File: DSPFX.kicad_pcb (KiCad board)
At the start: 2 copper layers, 182.8 x 128.5 mm, 151 parts, among them J10 Conn_02x05_Odd_Even, J101 AudioJack2, J102 AudioJack2, J103 AudioJack2, J104 AudioJack2, J105 Conn_02x04_Odd_Even, J106 AudioJack2, J107 AudioJack2, J108 AudioJack2, J109 AudioJack2, J110 AudioJack2, J111 AudioJack2, J112 AudioJack2, J113 AudioJack2_SwitchT, J114 Conn_02x04_Odd_Even, J115 Conn_01x04_Pin, J116 Conn_01x04_Pin, J117 Conn_01x04_Pin, J118 Conn_01x04_Pin, J119 Conn_01x04_Pin, J120 Conn_01x04_Pin, J121 Conn_01x03_Pin, J122 Conn_01x04_Pin, J123 Conn_01x02_Pin, J124 Conn_01x02_Pin, J125 Conn_01x03_Pin, J126 Conn_01x04_Pin, J127 Conn_01x04_Pin, J128 Conn_01x04_Pin, Q101 BC847, Q102 BC847, Q103 BC847, Q104 BC847, SW101 SW_Push, SW102 SW_Push, U101 TL074, U102 MCP6004, U104 TL072, U105 7Segment, U106 LM337_SOT223, U107 DSP32-CORE

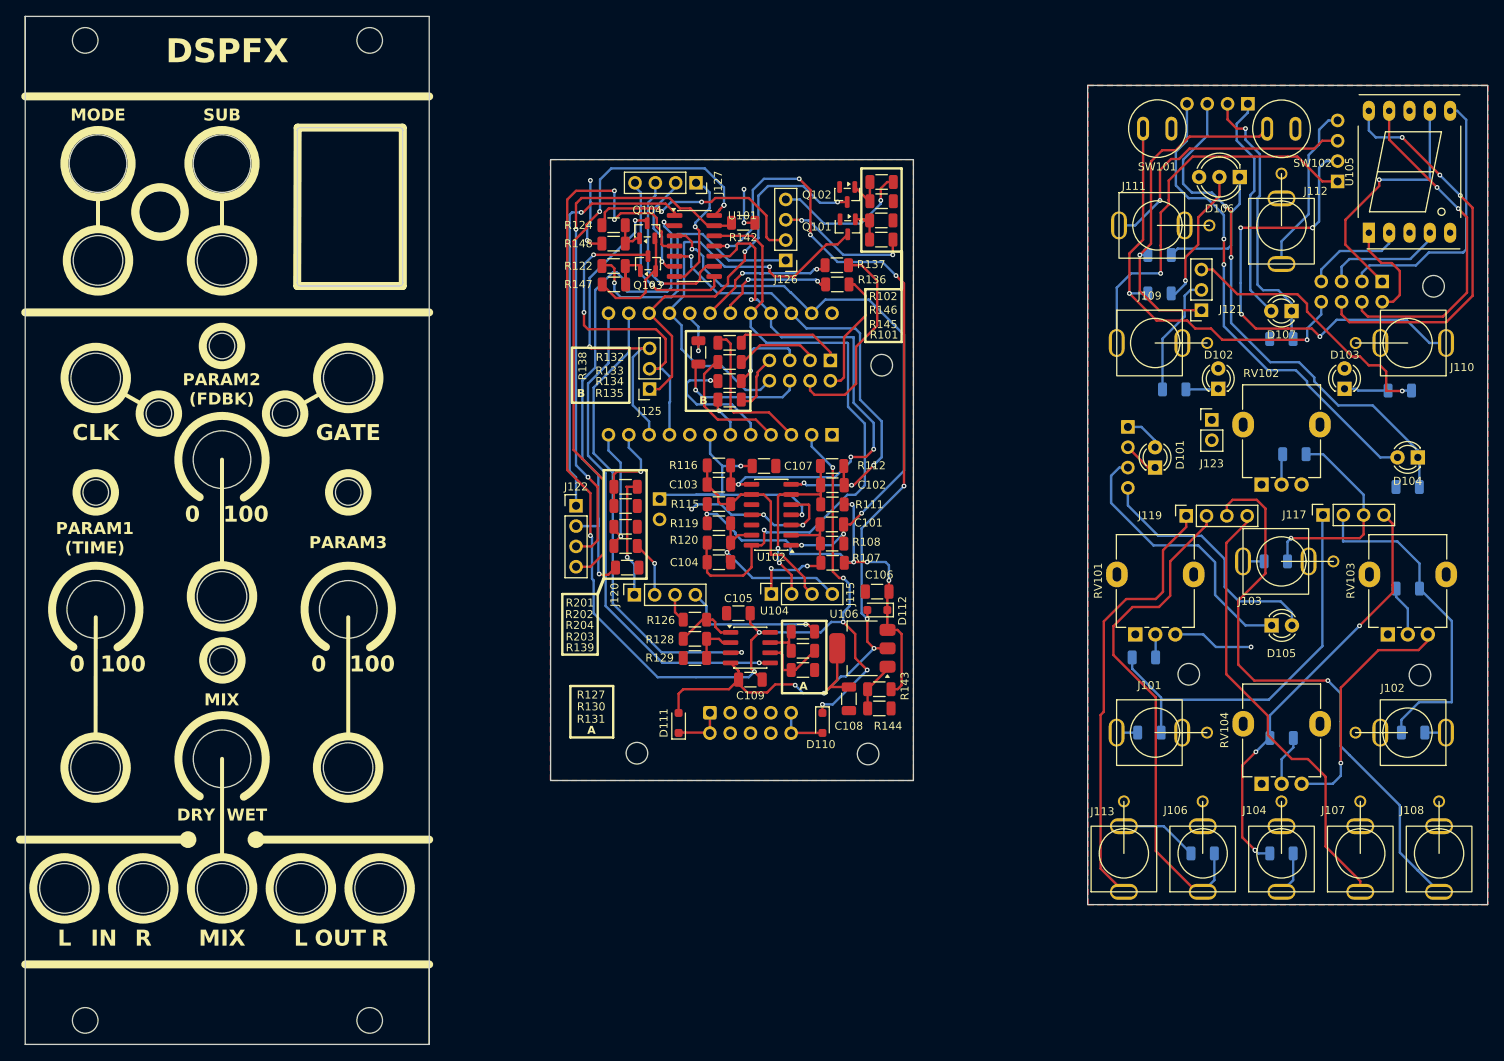
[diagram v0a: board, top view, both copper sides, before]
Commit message: Swapped LEDs and Potentiometer parity issue
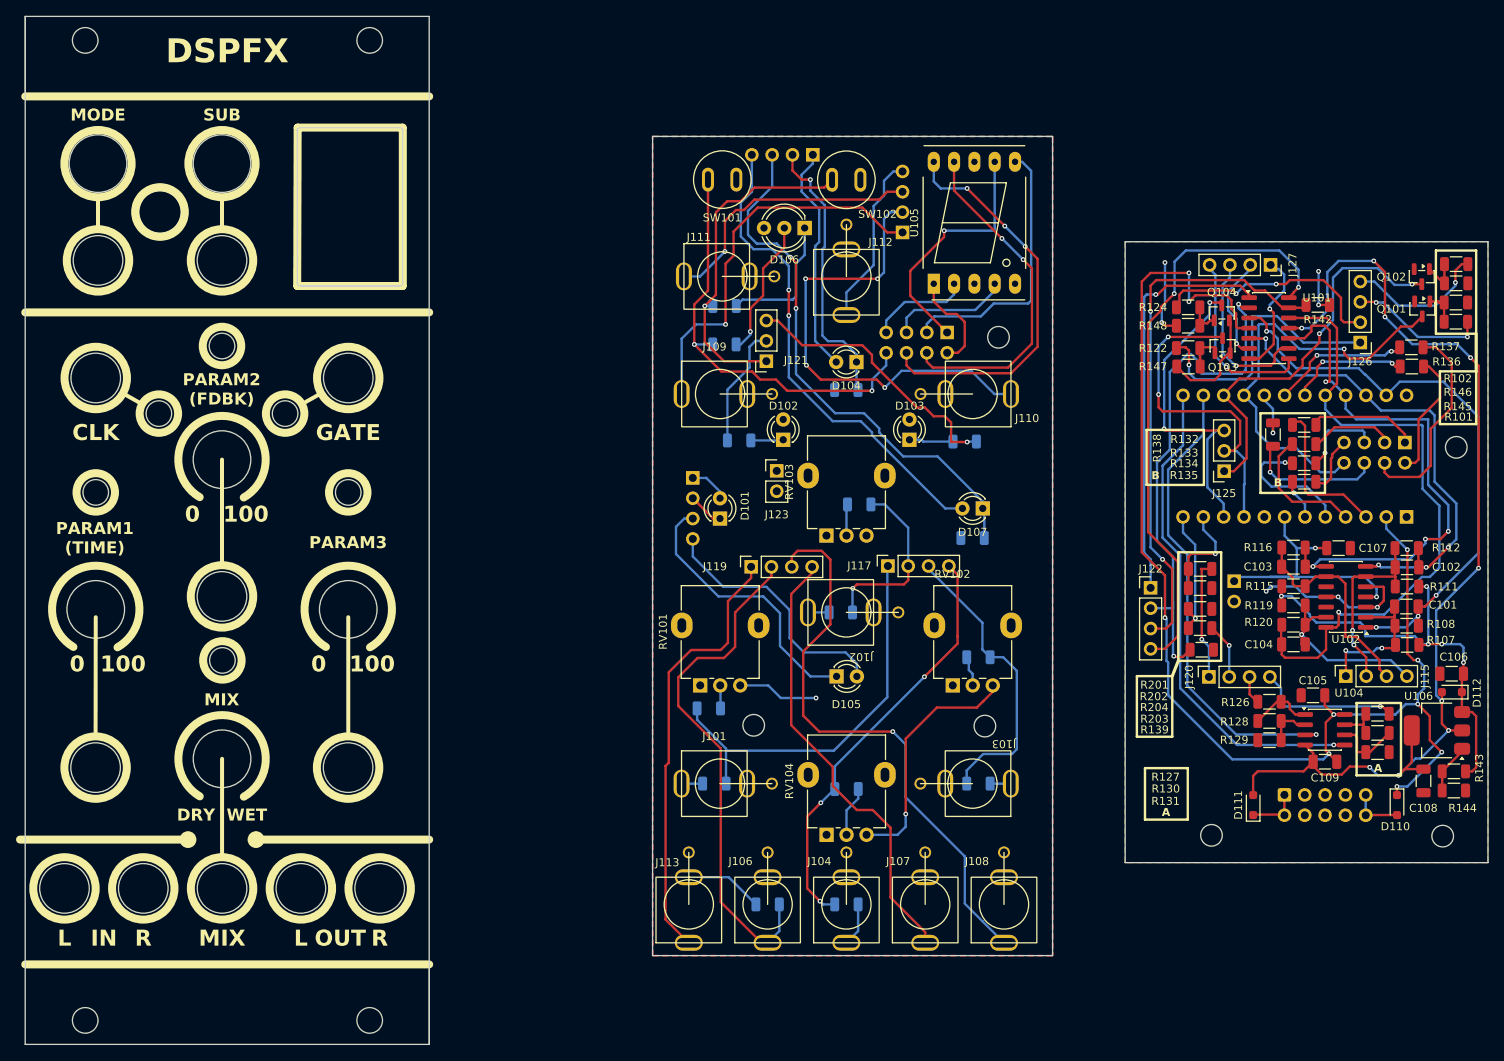
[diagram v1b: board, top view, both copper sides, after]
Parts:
- moved R109 73.1 mm to (173.6, 100.7), turned to 180 degrees
- moved ? 72.5 mm to (248.8, 128.7)
- moved C101 72.5 mm to (244.3, 100.0)
- moved C106 72.5 mm to (250.0, 108.4)
- moved D111 72.5 mm to (225.1, 124.8)
- moved D112 72.5 mm to (250.0, 110.7)
- moved J114 72.5 mm to (244.1, 79.5)
- moved J115 72.5 mm to (236.7, 108.7)
- moved J120 72.5 mm to (219.6, 108.8)
- moved J125 72.5 mm to (221.5, 83.0)
- moved R102 72.5 mm to (250.5, 57.2)
- moved R107 72.5 mm to (244.4, 104.8)
- moved R108 72.5 mm to (244.3, 102.4)
- moved R112 72.5 mm to (244.3, 92.7)
- moved R122 72.5 mm to (217.0, 67.7)
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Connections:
- D104 pad 1: LEDN3 -> LEDN2
- D104 pad 2: LED3 -> LED2
- D107 pad 1: LEDN2 -> LEDN3
- D107 pad 2: LED2 -> LED3
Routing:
- net VGNDP2: track 64.9 -> 45.9 mm, vias 2 -> 3
- net VGNDP3: track 53.3 -> 63.8 mm, vias 1 -> 0
- net Net-(R110-Pad2): track 6.33 -> 3.66 mm
- net LED2: track 44.4 -> 43.5 mm
- net MODEJACK: track 51.0 -> 50.3 mm
- net Net-(U107-INL): track 15.5 -> 14.8 mm
- net Net-(U107-GPIO40): track 6.41 -> 5.79 mm
- net Net-(Q104-B): track 4.76 -> 4.24 mm
- net LEDN4: track 101.5 -> 100.9 mm
- net VGNDM: vias 5 -> 4
- net GATEJACK: vias 7 -> 6
- net LED4: vias 3 -> 2
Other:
- outline, holes or cut-outs redrawn
